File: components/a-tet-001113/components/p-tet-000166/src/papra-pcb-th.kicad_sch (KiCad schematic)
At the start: 36 parts, among them IC1 78Z, Q1 NMOSFET, Q2 FQP27P06, Q3 NMOSFET, U2 QT Py ESP32-S3

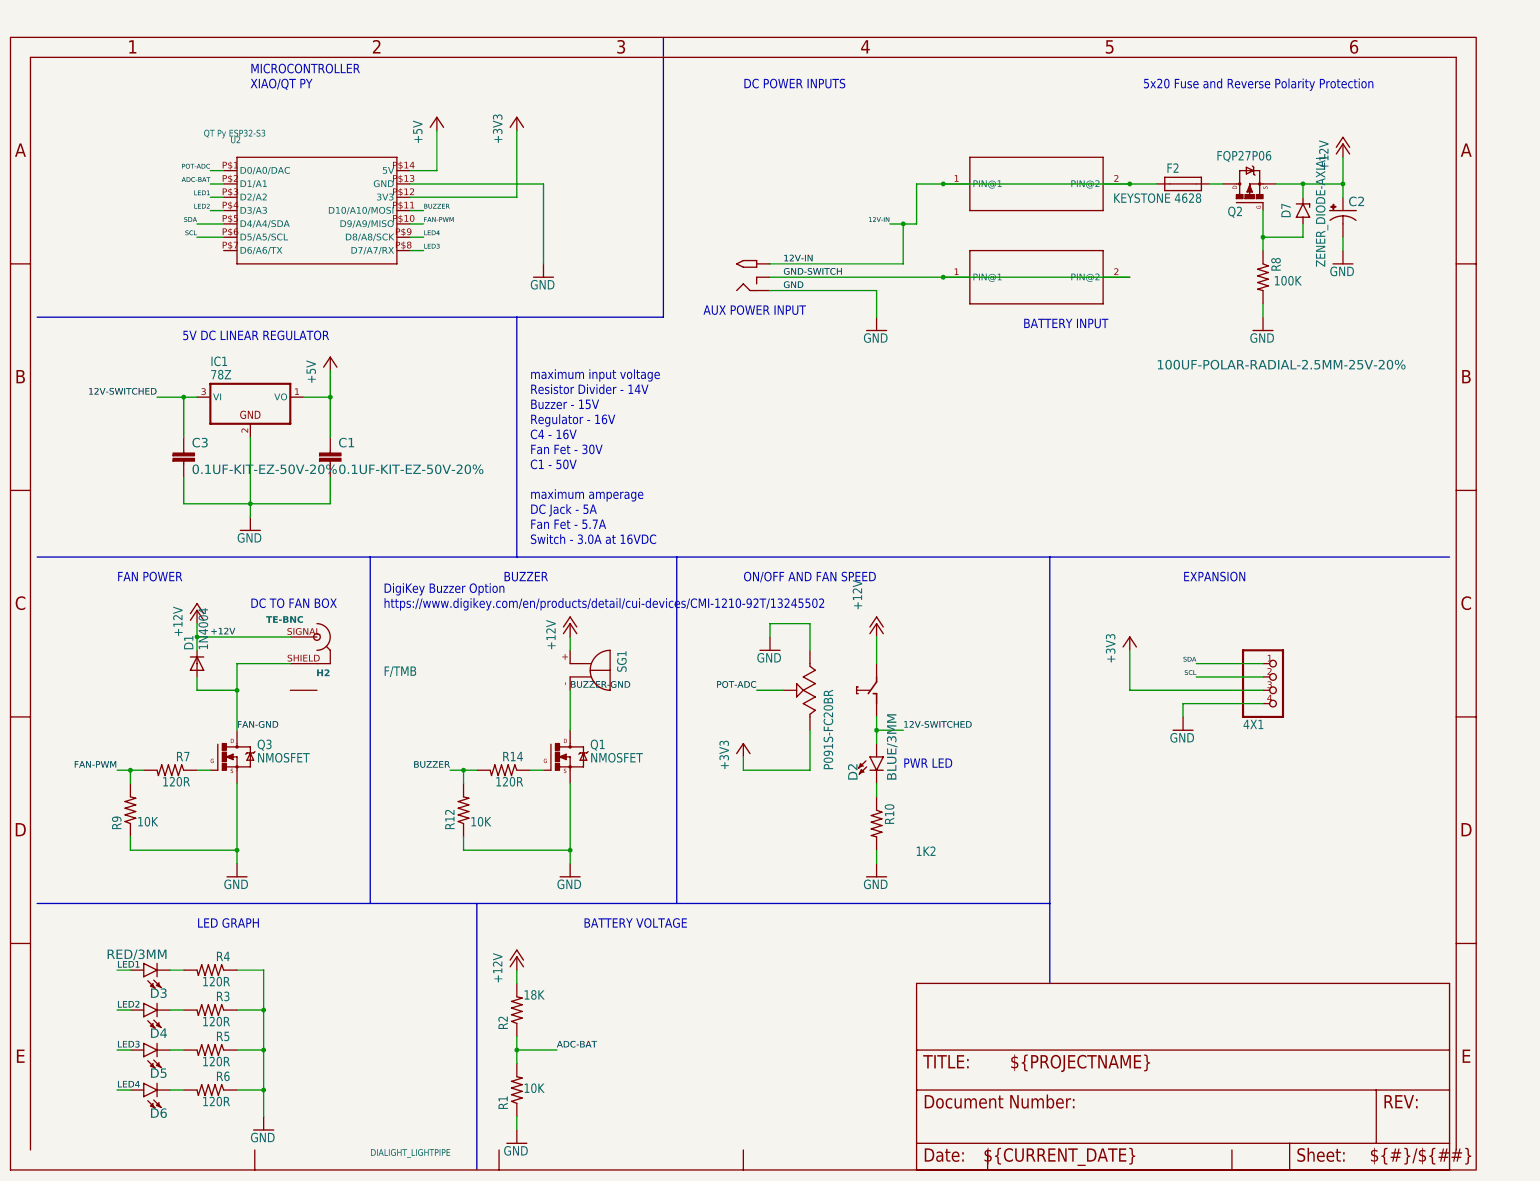
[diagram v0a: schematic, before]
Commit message: attempting to resolve footprints
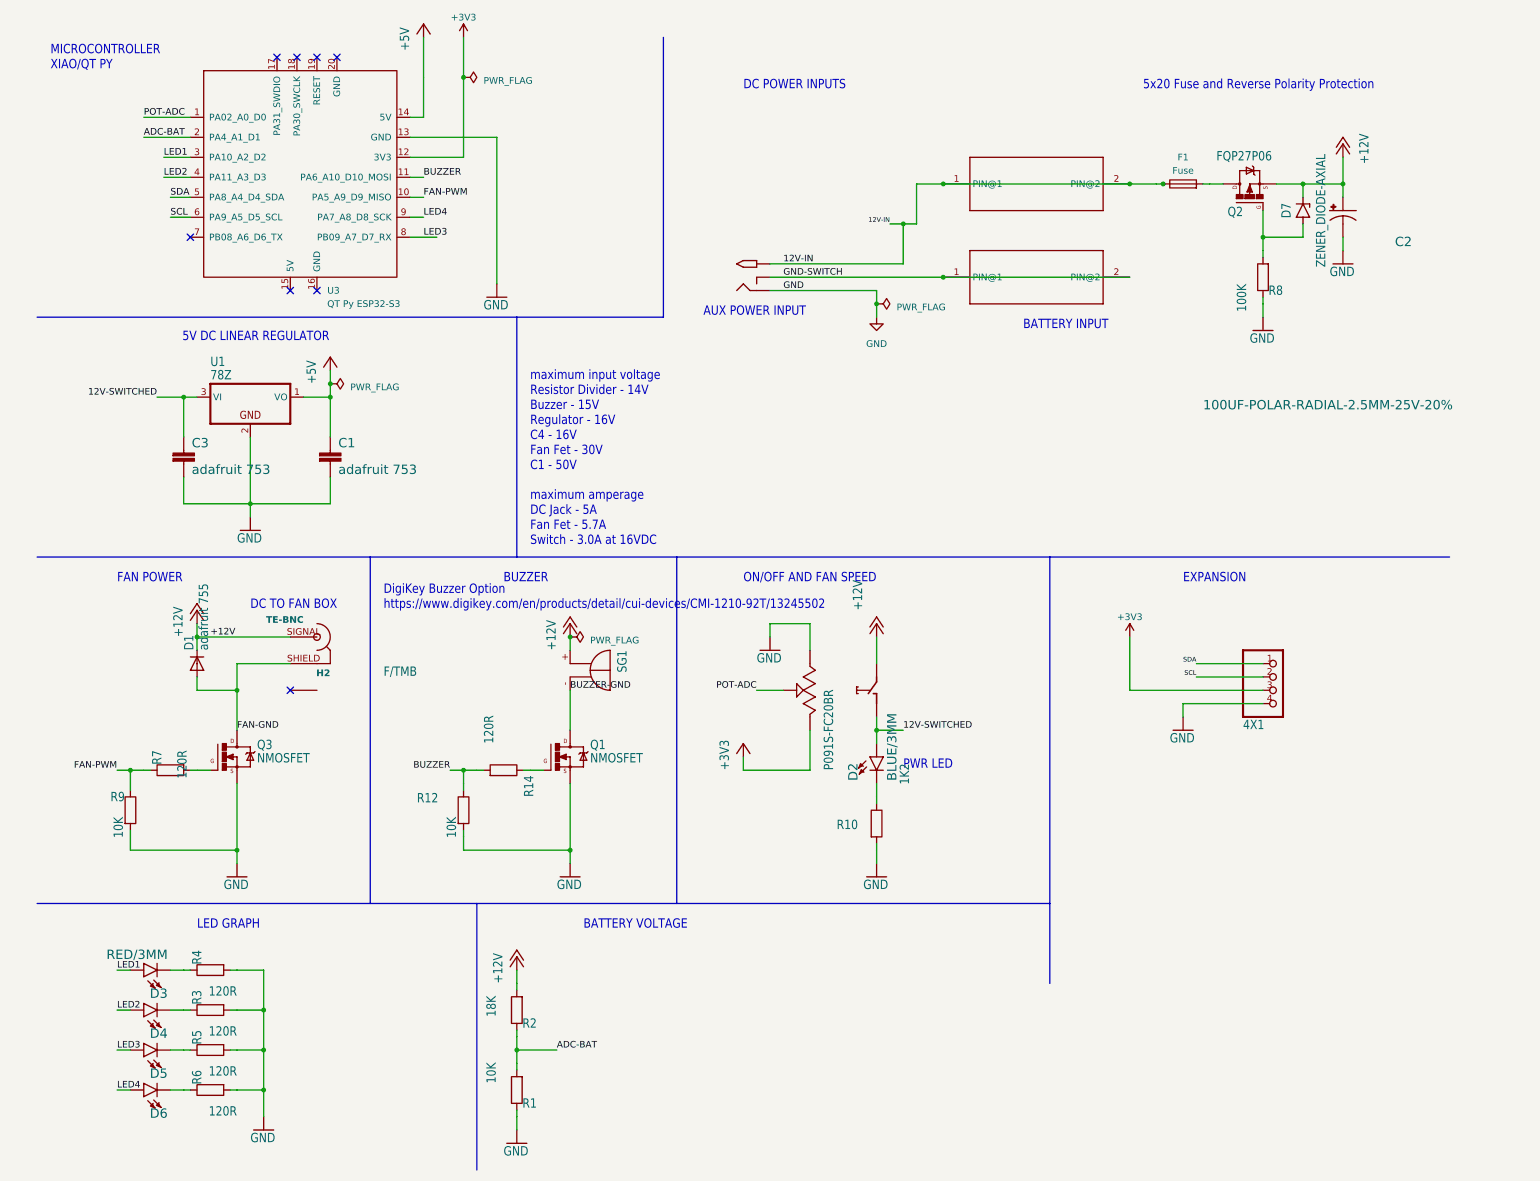
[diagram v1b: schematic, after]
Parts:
- removed F2: KEYSTONE 4628, Papra TH v1.0:FH_5X20, symbol Papra TH v1.0-eagle-import:FH_5X20
- removed U2: QT Py ESP32-S3, Papra TH v1.0:MODULE14P-TH+PAD, symbol Papra TH v1.0-eagle-import:MOUDLE-SEEEDUINO-XIAOTHRUHOLE+CASTELLATION
- added F1: Fuse, symbol Device:Fuse
- added U3: QT Py ESP32-S3, Seeeduino-XAIO:Seeeduino XIAO-MOUDLE14P-2.54-21X17.8MM, symbol Seeeduino-XAIO:SeeeduinoXIAO
- C1, C3: value 0.1UF-KIT-EZ-50V-20% -> adafruit 753; footprint Papra TH v1.0:CAP-PTH-SMALL-KIT -> Capacitor_THT:C_Rect_L4.0mm_W2.5mm_P2.50mm
- C2: footprint Papra TH v1.0:CPOL-RADIAL-2.5MM-6.5MM -> Capacitor_THT:CP_Radial_D5.0mm_P2.50mm; Alternate P/N (none) -> panasonic eca-1chg101i
- D1: value 1N4004 -> adafruit 755; footprint Papra TH v1.0:DO41-10 -> Diode_THT:D_DO-41_SOD81_P10.16mm_Horizontal; P/N (none) -> 1n4001
- D2, D3, D4, D5, D6: footprint Papra TH v1.0:LED_3MM -> LED_THT:LED_D5.0mm
- D7: footprint Papra TH v1.0:DIODE-AXIAL -> Diode_THT:D_DO-41_SOD81_P10.16mm_Horizontal
- H3: renamed from U$1; footprint Papra TH v1.0:01X4 -> Connector_PinHeader_2.54mm:PinHeader_1x04_P2.54mm_Vertical
- LP1: footprint Papra TH v1.0:DIALIGHT_5151020F__LEDS -> (none)
- Q1, Q2, Q3: footprint Papra TH v1.0:TO220BV -> Package_TO_SOT_THT:TO-220-3_Vertical
- R1, R12, R14, R2, R3, R4, R5, R6, R7, R8, R9: footprint Papra TH v1.0:0207_12 -> Resistor_THT:R_Axial_DIN0207_L6.3mm_D2.5mm_P10.16mm_Horizontal; symbol Papra TH v1.0-eagle-import:R-US_0207/12 -> Device:R
- R10: symbol Papra TH v1.0-eagle-import:R-US_0207/12 -> Device:R
- SG1: footprint Papra TH v1.0:F_TMB -> (none)
- U1: renamed from IC1; footprint Papra TH v1.0:TO92 -> Package_TO_SOT_THT:TO-92_HandSolder
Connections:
- net +3V3: now also U3.12 (3V3)
- net +5V: now also U3.14 (5V)
- net 12V-IN: now also F1.1
- net ADC-BAT: now also U3.2 (PA4_A1_D1)
- net BUZZER: now also R12.1, U3.11 (PA6_A10_D10_MOSI); no longer R12.2
- net FAN-PWM: now also R7.1, R9.1, U3.10 (PA5_A9_D9_MISO); no longer R7.2, R9.2
- net GND: now also R12.2, R3.2, R4.2, R5.2, R6.2, R8.1, R9.2, U3.13 (GND); no longer R12.1, R3.1, R4.1, R5.1, R6.1, R8.2, R9.1
- net LED1: now also U3.3 (PA10_A2_D2)
- net LED2: now also U3.4 (PA11_A3_D3)
- net LED3: now also U3.8 (PB09_A7_D7_RX)
- net LED4: now also U3.9 (PA7_A8_D8_SCK)
- net POT-ADC: now also U3.1 (PA02_A0_D0)
- net SCL: now also U3.6 (PA9_A5_D5_SCL)
- net SDA: now also U3.5 (PA8_A4_D4_SDA)
- net at D5.K (C): now also R5.1; no longer R5.2
- net at Q3.G: now also R7.2; no longer R7.1
- net at Q2.D: now also F1.2
- net at D3.K (C): now also R4.1; no longer R4.2
- net at D4.K (C): now also R3.1; no longer R3.2
- net at D6.K (C): now also R6.1; no longer R6.2
- net at D7.1 (A), Q2.G: now also R8.2; no longer R8.1
- no-connect marks 0 -> 8
